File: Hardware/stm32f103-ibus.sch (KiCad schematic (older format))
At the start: 23 parts

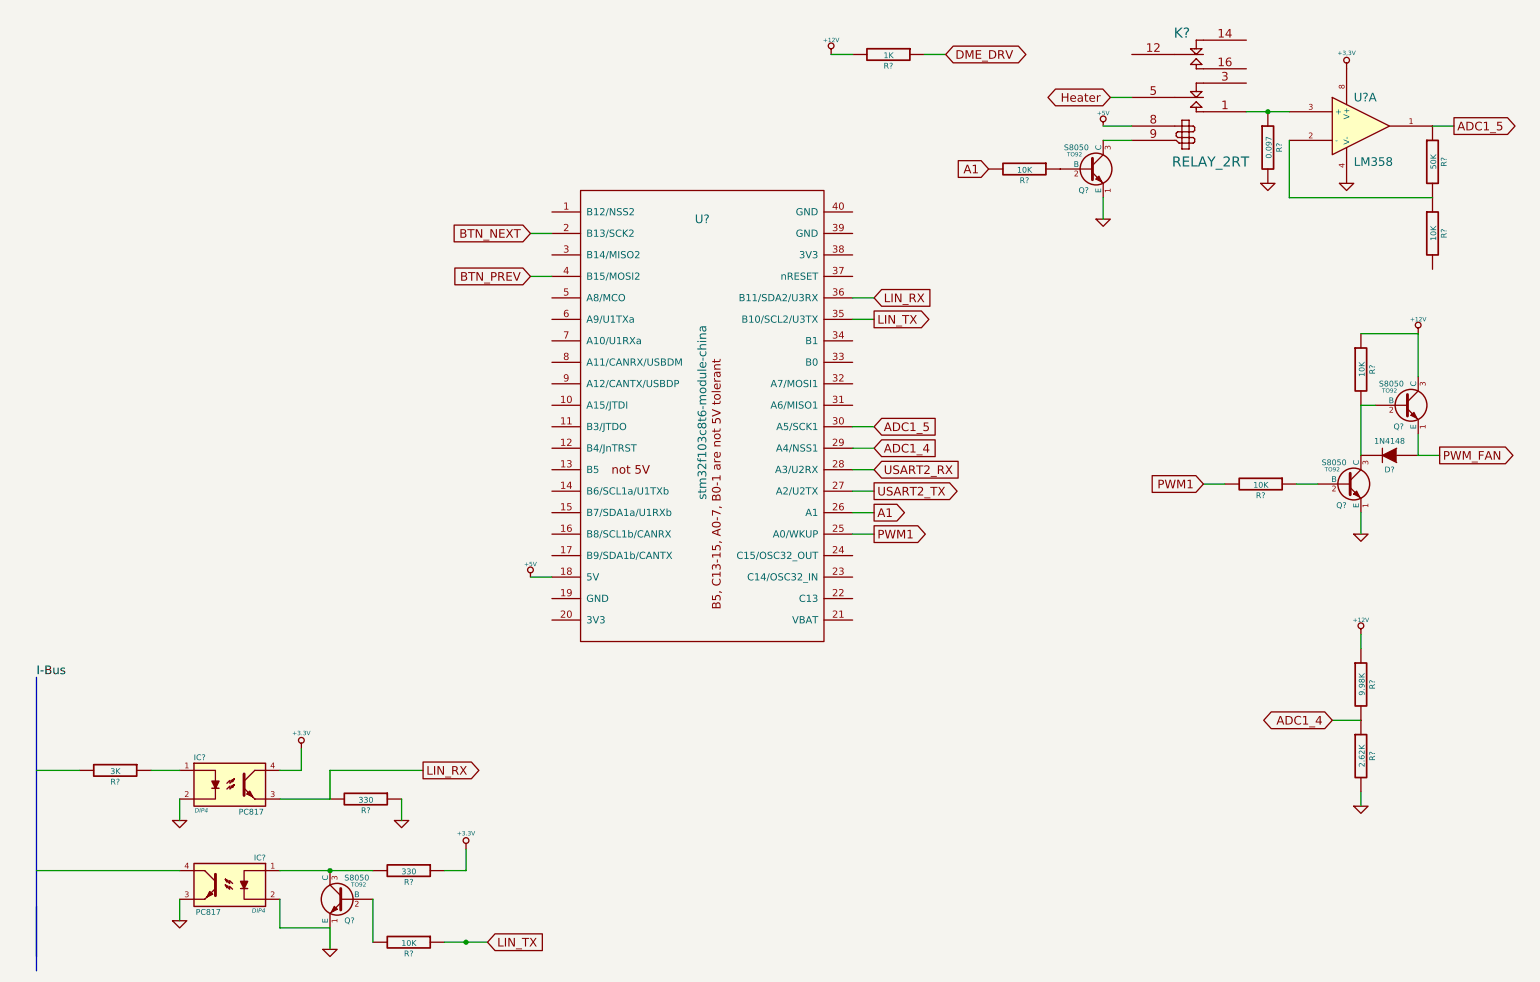
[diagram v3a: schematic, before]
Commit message: 1.Remove Hardware/stm32f103-ibus.bak 2.Modify of schematic 3.Force heater off while heater current over 2A 4.Modify logic of target temperature compensation 5.Add License
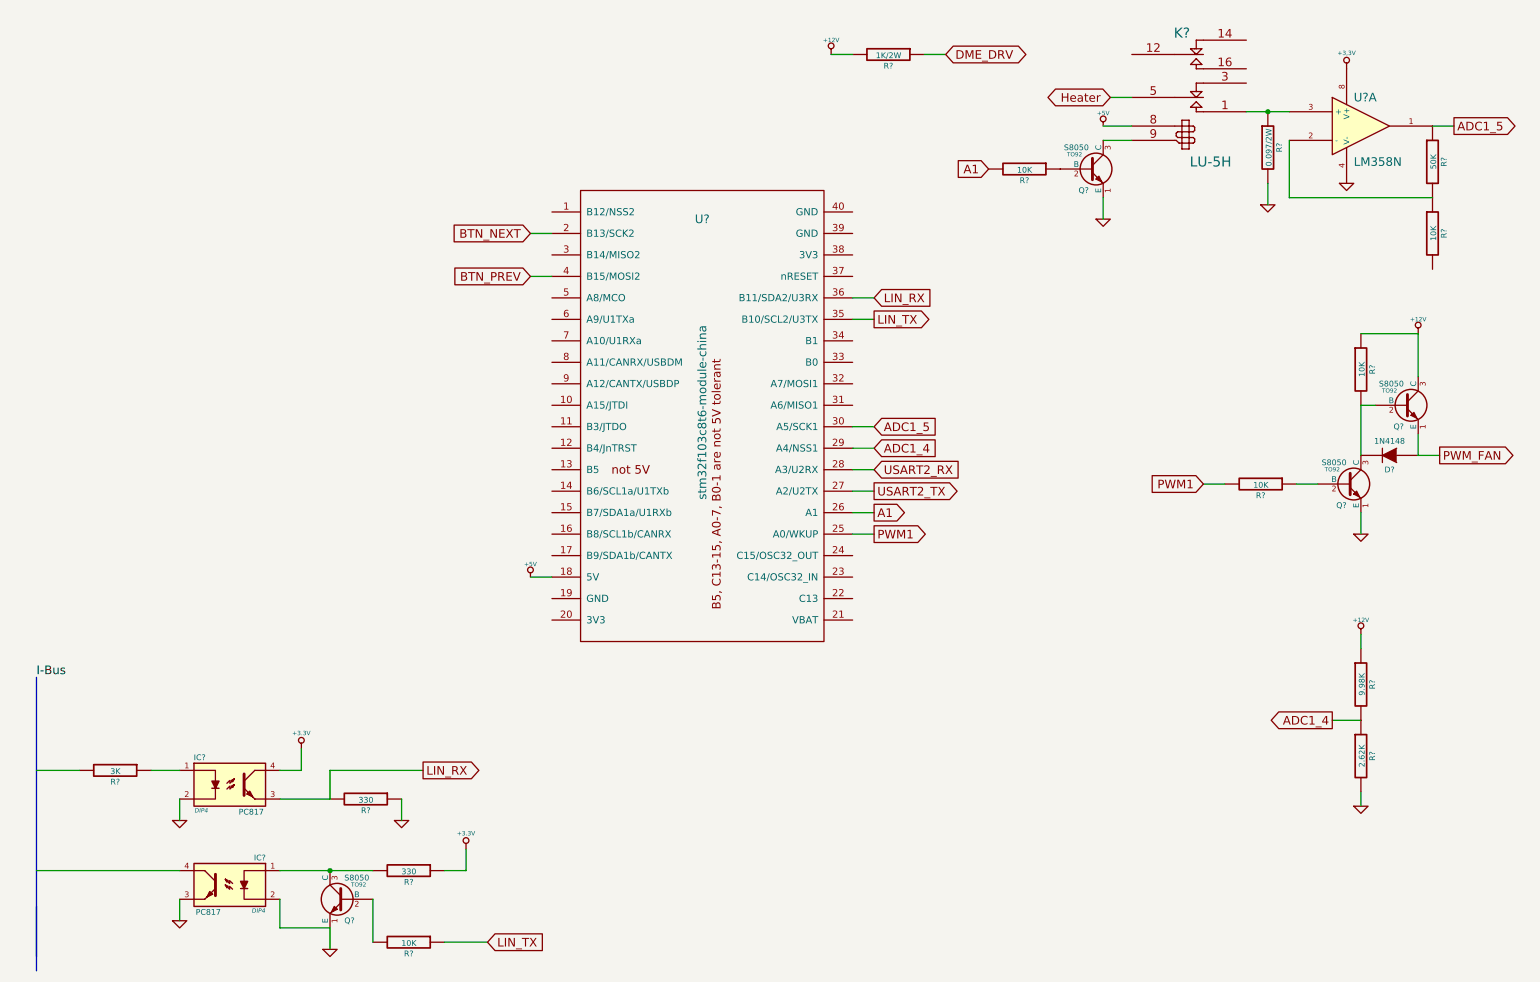
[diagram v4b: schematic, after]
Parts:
- K?: value RELAY_2RT -> LU-5H
- R?: value 1K -> 1K/2W
- R?: value 0.097 -> 0.097/2W
- U?: value LM358 -> LM358N
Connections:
- wire segments 52 -> 53
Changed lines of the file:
@@
 	1    0    0    -1
 $EndComp
-Text GLabel 9850 5600 0    60   BiDi ~ 0
+Text GLabel 9850 5600 0    60   Output ~ 0
 ADC1_4
 Text GLabel 8300 1250 0    60   BiDi ~ 0
@@
 P 6750 950
 F 0 "R?" V 6830 950 40  0000 C CNN
-F 1 "1K" V 6757 951 40  0000 C CNN
+F 1 "1K/2W" V 6757 951 40  0000 C CNN
 F 2 "" V 6680 950 30  0000 C CNN
 F 3 "" H 6750 950 30  0000 C CNN
@@
 P 8850 1200
 F 0 "K?" H 8800 1600 70  0000 C CNN
-F 1 "RELAY_2RT" H 9000 700 70  0000 C CNN
+F 1 "LU-5H" H 9000 700 70  0000 C CNN
 F 2 "" H 8850 1200 60  0000 C CNN
 F 3 "" H 8850 1200 60  0000 C CNN
@@
 P 10050 1450
 F 0 "U?" H 10000 1650 60  0000 L CNN
-F 1 "LM358" H 10000 1200 60  0000 L CNN
+F 1 "LM358N" H 10000 1200 60  0000 L CNN
 F 2 "" H 10050 1450 60  0000 C CNN
 F 3 "" H 10050 1450 60  0000 C CNN
@@
 $EndComp
 $Comp
-L GND #PWR?
-U 1 1 59957459
-P 9400 1850
-F 0 "#PWR?" H 9400 1850 30  0001 C CNN
-F 1 "GND" H 9400 1780 30  0001 C CNN
-F 2 "" H 9400 1850 60  0000 C CNN
-F 3 "" H 9400 1850 60  0000 C CNN
-	1    9400 1850
+L R R?
+U 1 1 599587F4
+P 9400 1600
+F 0 "R?" V 9480 1600 40  0000 C CNN
+F 1 "0.097/2W" V 9407 1601 40  0000 C CNN
+F 2 "" V 9330 1600 30  0000 C CNN
+F 3 "" H 9400 1600 30  0000 C CNN
+	1    9400 1600
 	1    0    0    -1
 $EndComp
@@
 	3150 6850 3150 7150
 Wire Wire Line
+	3650 6650 3800 6650
+Wire Wire Line
+	3800 6650 3800 6500
+Wire Wire Line
+	2850 7050 2850 7200
+Wire Wire Line
+	2500 6850 2500 7050
+Wire Wire Line
+	2500 7050 2850 7050
+Wire Wire Line
+	1800 6850 1800 7000
+Wire Wire Line
+	6500 2650 6650 2650
+Wire Wire Line
+	6500 2800 6650 2800
+Wire Wire Line
+	6500 3850 6650 3850
+Wire Wire Line
+	6500 4000 6650 4000
+Wire Wire Line
+	3350 6150 3350 6300
+Wire Wire Line
+	6500 3700 6650 3700
+Wire Wire Line
+	10050 5000 10050 5100
+Wire Wire Line
+	10050 6100 10050 6200
+Wire Wire Line
+	9850 5600 10050 5600
+Wire Wire Line
+	8250 1950 8250 2100
+Wire Wire Line
+	8250 1550 8450 1550
+Wire Wire Line
+	8250 1450 8450 1450
+Wire Wire Line
+	6500 950  6350 950
+Wire Wire Line
+	6650 4300 6500 4300
+Wire Wire Line
+	6650 4150 6500 4150
+Wire Wire Line
+	7000 950  7150 950
+Wire Wire Line
+	8300 1250 8450 1250
+Wire Wire Line
+	4400 4600 4250 4600
+Wire Wire Line
+	10450 2900 10050 2900
+Wire Wire Line
+	10050 3400 10150 3400
+Wire Wire Line
+	10450 2900 10450 3200
+Wire Wire Line
+	10050 3400 10050 3750
+Wire Wire Line
+	10450 3600 10450 3750
+Wire Wire Line
+	8950 3950 9100 3950
+Wire Wire Line
+	9600 3950 9750 3950
+Wire Wire Line
+	10050 4150 10050 4300
+Wire Wire Line
+	10450 3750 10600 3750
+Wire Wire Line
+	4250 2200 4400 2200
+Wire Wire Line
+	4250 2500 4400 2500
+Wire Wire Line
+	6500 3550 6650 3550
+Wire Wire Line
+	10700 1450 10550 1450
+Wire Wire Line
+	9550 1550 9550 1950
+Wire Wire Line
+	9550 1950 10550 1950
+Wire Wire Line
+	2500 6150 2850 6150
+Wire Wire Line
+	3500 5950 2850 5950
+Wire Wire Line
+	2850 5950 2850 6150
+Wire Wire Line
+	3950 7150 3650 7150
+Wire Wire Line
 	2500 6650 3150 6650
 Connection ~ 2850 6650
 Wire Wire Line
-	3650 6650 3800 6650
-Wire Wire Line
-	3650 7150 3950 7150
-Connection ~ 3800 7150
-Wire Wire Line
-	3800 6650 3800 6500
-Wire Wire Line
-	2850 7050 2850 7200
-Wire Wire Line
-	2500 6850 2500 7050
-Wire Wire Line
-	2500 7050 2850 7050
-Wire Wire Line
-	1800 6850 1800 7000
-Wire Wire Line
-	6500 2650 6650 2650
-Wire Wire Line
-	6500 2800 6650 2800
-Wire Wire Line
-	6500 3850 6650 3850
-Wire Wire Line
-	6500 4000 6650 4000
-Wire Wire Line
-	2500 6150 2850 6150
-Wire Wire Line
-	2850 6150 2850 5950
-Wire Wire Line
-	2850 5950 3500 5950
-Wire Wire Line
-	3350 6150 3350 6300
-Wire Wire Line
-	6500 3700 6650 3700
-Wire Wire Line
-	10050 5000 10050 5100
-Wire Wire Line
-	10050 6100 10050 6200
-Wire Wire Line
-	9850 5600 10050 5600
-Wire Wire Line
-	8250 1950 8250 2100
-Wire Wire Line
-	8250 1550 8450 1550
-Wire Wire Line
-	8250 1450 8450 1450
-Wire Wire Line
-	6500 950  6350 950
-Wire Wire Line
-	6650 4300 6500 4300
-Wire Wire Line
-	6650 4150 6500 4150
-Wire Wire Line
-	7000 950  7150 950
-Wire Wire Line
-	8300 1250 8450 1250
-Wire Wire Line
-	4400 4600 4250 4600
-Wire Wire Line
-	10450 2900 10050 2900
-Wire Wire Line
-	10050 3400 10150 3400
-Wire Wire Line
-	10450 2900 10450 3200
-Wire Wire Line
-	10050 3400 10050 3750
-Wire Wire Line
-	10450 3600 10450 3750
-Wire Wire Line
-	8950 3950 9100 3950
-Wire Wire Line
-	9600 3950 9750 3950
-Wire Wire Line
-	10050 4150 10050 4300
-Wire Wire Line
-	10450 3750 10600 3750
-Wire Wire Line
-	4250 2200 4400 2200
-Wire Wire Line
-	4250 2500 4400 2500
-Wire Wire Line
-	6500 3550 6650 3550
-Wire Wire Line
-	10700 1450 10550 1450
-Wire Wire Line
-	9550 1550 9550 1950
-Wire Wire Line
-	9550 1950 10550 1950
-$Comp
-L R R?
-U 1 1 599587F4
-P 9400 1600
-F 0 "R?" V 9480 1600 40  0000 C CNN
-F 1 "0.097" V 9407 1601 40  0000 C CNN
-F 2 "" V 9330 1600 30  0000 C CNN
-F 3 "" H 9400 1600 30  0000 C CNN
-	1    9400 1600
-	1    0    0    -1
-$EndComp
-Wire Wire Line
 	9250 1350 9550 1350
 Connection ~ 9400 1350
+$Comp
+L GND #PWR?
+U 1 1 59A94DBE
+P 9400 2000
+F 0 "#PWR?" H 9400 2000 30  0001 C CNN
+F 1 "GND" H 9400 1930 30  0001 C CNN
+F 2 "" H 9400 2000 60  0000 C CNN
+F 3 "" H 9400 2000 60  0000 C CNN
+	1    9400 2000
+	1    0    0    -1
+$EndComp
+Wire Wire Line
+	9400 1850 9400 2000
 $EndSCHEMATC

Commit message: 1.Add connector to schematic 2.Remove NEXT_BTN / PREV_BTN of schematic
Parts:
- added P?: USART2, symbol CONN_01X04
- added P?: POWER, symbol CONN_01X02
- added P?: I-Bus, symbol CONN_01X01
- added P?: HEATER, symbol CONN_01X01
- added P?: PWM_FAN, symbol CONN_01X01
- added P?: DME_DRV, symbol CONN_01X01
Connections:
- net labels added: HEATER
- net labels removed: BTN_NEXT, BTN_PREV, Heater
- wire segments 53 -> 64
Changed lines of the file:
@@
 ADC1_4
 Text GLabel 8300 1250 0    60   BiDi ~ 0
-Heater
+HEATER
 $Comp
 L S8050 Q?
@@
 Text GLabel 6650 3550 2    60   Input ~ 0
 ADC1_5
-Text GLabel 4250 2200 0    60   Input ~ 0
-BTN_NEXT
-Text GLabel 4250 2500 0    60   Input ~ 0
-BTN_PREV
 $Comp
 L LM358 U?
@@
 	1    0    0    -1
 $EndComp
-Wire Bus Line
-	800  5300 800  7250
-Wire Bus Line
-	800  6900 800  7350
-Wire Wire Line
-	800  5950 1100 5950
-Wire Wire Line
-	1600 5950 1800 5950
-Wire Wire Line
-	1800 6150 1800 6300
-Wire Wire Line
-	2500 5950 2650 5950
-Wire Wire Line
-	2650 5950 2650 5800
-Wire Wire Line
-	800  6650 1800 6650
-Wire Wire Line
-	3150 6850 3150 7150
-Wire Wire Line
-	3650 6650 3800 6650
-Wire Wire Line
-	3800 6650 3800 6500
-Wire Wire Line
-	2850 7050 2850 7200
-Wire Wire Line
-	2500 6850 2500 7050
-Wire Wire Line
-	2500 7050 2850 7050
-Wire Wire Line
-	1800 6850 1800 7000
-Wire Wire Line
-	6500 2650 6650 2650
-Wire Wire Line
-	6500 2800 6650 2800
-Wire Wire Line
-	6500 3850 6650 3850
-Wire Wire Line
-	6500 4000 6650 4000
-Wire Wire Line
-	3350 6150 3350 6300
-Wire Wire Line
-	6500 3700 6650 3700
-Wire Wire Line
-	10050 5000 10050 5100
-Wire Wire Line
-	10050 6100 10050 6200
-Wire Wire Line
-	9850 5600 10050 5600
-Wire Wire Line
-	8250 1950 8250 2100
-Wire Wire Line
-	8250 1550 8450 1550
-Wire Wire Line
-	8250 1450 8450 1450
-Wire Wire Line
-	6500 950  6350 950
-Wire Wire Line
-	6650 4300 6500 4300
-Wire Wire Line
-	6650 4150 6500 4150
-Wire Wire Line
-	7000 950  7150 950
-Wire Wire Line
-	8300 1250 8450 1250
-Wire Wire Line
-	4400 4600 4250 4600
-Wire Wire Line
-	10450 2900 10050 2900
-Wire Wire Line
-	10050 3400 10150 3400
-Wire Wire Line
-	10450 2900 10450 3200
-Wire Wire Line
-	10050 3400 10050 3750
-Wire Wire Line
-	10450 3600 10450 3750
-Wire Wire Line
-	8950 3950 9100 3950
-Wire Wire Line
-	9600 3950 9750 3950
-Wire Wire Line
-	10050 4150 10050 4300
-Wire Wire Line
-	10450 3750 10600 3750
-Wire Wire Line
-	4250 2200 4400 2200
-Wire Wire Line
-	4250 2500 4400 2500
-Wire Wire Line
-	6500 3550 6650 3550
-Wire Wire Line
-	10700 1450 10550 1450
-Wire Wire Line
-	9550 1550 9550 1950
-Wire Wire Line
-	9550 1950 10550 1950
-Wire Wire Line
-	2500 6150 2850 6150
-Wire Wire Line
-	3500 5950 2850 5950
-Wire Wire Line
-	2850 5950 2850 6150
-Wire Wire Line
-	3950 7150 3650 7150
-Wire Wire Line
-	2500 6650 3150 6650
-Connection ~ 2850 6650
-Wire Wire Line
-	9250 1350 9550 1350
-Connection ~ 9400 1350
 $Comp
 L GND #PWR?
@@
 	1    0    0    -1
 $EndComp
+$Comp
+L CONN_01X04 P?
+U 1 1 59AF8F34
+P 850 950
+F 0 "P?" H 850 1200 50  0000 C CNN
+F 1 "USART2" V 950 950 50  0000 C CNN
+F 2 "" H 850 950 60  0000 C CNN
+F 3 "" H 850 950 60  0000 C CNN
+	1    850  950
+	-1   0    0    -1
+$EndComp
+$Comp
+L +3.3V #PWR?
+U 1 1 59AF94A8
+P 1200 800
+F 0 "#PWR?" H 1200 760 30  0001 C CNN
+F 1 "+3.3V" H 1200 910 30  0000 C CNN
+F 2 "" H 1200 800 60  0000 C CNN
+F 3 "" H 1200 800 60  0000 C CNN
+	1    1200 800
+	1    0    0    -1
+$EndComp
+$Comp
+L GND #PWR?
+U 1 1 59AF94BC
+P 1050 1250
+F 0 "#PWR?" H 1050 1250 30  0001 C CNN
+F 1 "GND" H 1050 1180 30  0001 C CNN
+F 2 "" H 1050 1250 60  0000 C CNN
+F 3 "" H 1050 1250 60  0000 C CNN
+	1    1050 1250
+	1    0    0    -1
+$EndComp
+Text GLabel 1350 1100 2    60   Input ~ 0
+USART2_TX
+Text GLabel 1200 900  2    60   Output ~ 0
+USART2_RX
+$Comp
+L CONN_01X02 P?
+U 1 1 59AFA389
+P 850 1600
+F 0 "P?" H 850 1750 50  0000 C CNN
+F 1 "POWER" V 950 1600 50  0000 C CNN
+F 2 "" H 850 1600 60  0000 C CNN
+F 3 "" H 850 1600 60  0000 C CNN
+	1    850  1600
+	-1   0    0    -1
+$EndComp
+$Comp
+L +12V #PWR?
+U 1 1 59AFA45F
+P 1200 1550
+F 0 "#PWR?" H 1200 1500 20  0001 C CNN
+F 1 "+12V" H 1200 1650 30  0000 C CNN
+F 2 "" H 1200 1550 60  0000 C CNN
+F 3 "" H 1200 1550 60  0000 C CNN
+	1    1200 1550
+	1    0    0    -1
+$EndComp
+$Comp
+L GND #PWR?
+U 1 1 59AFA473
+P 1200 1750
+F 0 "#PWR?" H 1200 1750 30  0001 C CNN
+F 1 "GND" H 1200 1680 30  0001 C CNN
+F 2 "" H 1200 1750 60  0000 C CNN
+F 3 "" H 1200 1750 60  0000 C CNN
+	1    1200 1750
+	1    0    0    -1
+$EndComp
+$Comp
+L CONN_01X01 P?
+U 1 1 59AFA583
+P 850 2050
+F 0 "P?" H 850 2150 50  0000 C CNN
+F 1 "I-Bus" V 950 2050 50  0000 C CNN
+F 2 "" H 850 2050 60  0000 C CNN
+F 3 "" H 850 2050 60  0000 C CNN
+	1    850  2050
+	-1   0    0    -1
+$EndComp
+$Comp
+L CONN_01X01 P?
+U 1 1 59AFA59E
+P 850 2500
+F 0 "P?" H 850 2600 50  0000 C CNN
+F 1 "HEATER" V 950 2500 50  0000 C CNN
+F 2 "" H 850 2500 60  0000 C CNN
+F 3 "" H 850 2500 60  0000 C CNN
+	1    850  2500
+	-1   0    0    -1
+$EndComp
+Wire Bus Line
+	800  5300 800  7250
+Wire Bus Line
+	800  6900 800  7350
+Wire Wire Line
+	800  5950 1100 5950
+Wire Wire Line
+	1600 5950 1800 5950
+Wire Wire Line
+	1800 6150 1800 6300
+Wire Wire Line
+	2500 5950 2650 5950
+Wire Wire Line
+	2650 5950 2650 5800
+Wire Wire Line
+	800  6650 1800 6650
+Wire Wire Line
+	3150 6850 3150 7150
+Wire Wire Line
+	3650 6650 3800 6650
+Wire Wire Line
+	3800 6650 3800 6500
+Wire Wire Line
+	2850 7050 2850 7200
+Wire Wire Line
+	2500 6850 2500 7050
+Wire Wire Line
+	2500 7050 2850 7050
+Wire Wire Line
+	1800 6850 1800 7000
+Wire Wire Line
+	6500 2650 6650 2650
+Wire Wire Line
+	6500 2800 6650 2800
+Wire Wire Line
+	6500 3850 6650 3850
+Wire Wire Line
+	6500 4000 6650 4000
+Wire Wire Line
+	3350 6150 3350 6300
+Wire Wire Line
+	6500 3700 6650 3700
+Wire Wire Line
+	10050 5000 10050 5100
+Wire Wire Line
+	10050 6100 10050 6200
+Wire Wire Line
+	9850 5600 10050 5600
+Wire Wire Line
+	8250 1950 8250 2100
+Wire Wire Line
+	8250 1550 8450 1550
+Wire Wire Line
+	8250 1450 8450 1450
+Wire Wire Line
+	6500 950  6350 950
+Wire Wire Line
+	6650 4300 6500 4300
+Wire Wire Line
+	6650 4150 6500 4150
+Wire Wire Line
+	7000 950  7150 950
+Wire Wire Line
+	8300 1250 8450 1250
+Wire Wire Line
+	4400 4600 4250 4600
+Wire Wire Line
+	10450 2900 10050 2900
+Wire Wire Line
+	10050 3400 10150 3400
+Wire Wire Line
+	10450 2900 10450 3200
+Wire Wire Line
+	10050 3400 10050 3750
+Wire Wire Line
+	10450 3600 10450 3750
+Wire Wire Line
+	8950 3950 9100 3950
+Wire Wire Line
+	9600 3950 9750 3950
+Wire Wire Line
+	10050 4150 10050 4300
+Wire Wire Line
+	10450 3750 10600 3750
+Wire Wire Line
+	6500 3550 6650 3550
+Wire Wire Line
+	10700 1450 10550 1450
+Wire Wire Line
+	9550 1550 9550 1950
+Wire Wire Line
+	9550 1950 10550 1950
+Wire Wire Line
+	2500 6150 2850 6150
+Wire Wire Line
+	3500 5950 2850 5950
+Wire Wire Line
+	2850 5950 2850 6150
+Wire Wire Line
+	3950 7150 3650 7150
+Wire Wire Line
+	2500 6650 3150 6650
+Connection ~ 2850 6650
+Wire Wire Line
+	9250 1350 9550 1350
+Connection ~ 9400 1350
 Wire Wire Line
 	9400 1850 9400 2000
+Wire Wire Line
+	1050 800  1200 800
+Wire Wire Line
+	1050 1000 1200 1000
+Wire Wire Line
+	1200 1000 1200 1100
+Wire Wire Line
+	1050 900  1200 900
+Wire Wire Line
+	1200 1100 1350 1100
+Wire Wire Line
+	1050 1100 1050 1250
+Wire Wire Line
+	1050 1550 1200 1550
+Wire Wire Line
+	1050 1650 1200 1650
+Wire Wire Line
+	1200 1650 1200 1750
+Wire Bus Line
+	1500 1900 1500 2250
+Text Label 1500 2050 0    60   ~ 0
+I-Bus
+Wire Wire Line
+	1050 2050 1500 2050
+Text GLabel 1200 2500 2    60   BiDi ~ 0
+HEATER
+Wire Wire Line
+	1050 2500 1200 2500
+$Comp
+L CONN_01X01 P?
+U 1 1 59AFBA4B
+P 850 2950
+F 0 "P?" H 850 3050 50  0000 C CNN
+F 1 "PWM_FAN" V 950 2950 50  0000 C CNN
+F 2 "" H 850 2950 60  0000 C CNN
+F 3 "" H 850 2950 60  0000 C CNN
+	1    850  2950
+	-1   0    0    -1
+$EndComp
+Text GLabel 1200 2950 2    60   Input ~ 0
+PWM_FAN
+Wire Wire Line
+	1200 2950 1050 2950
+$Comp
+L CONN_01X01 P?
+U 1 1 59AFC60B
+P 850 3450
+F 0 "P?" H 850 3550 50  0000 C CNN
+F 1 "DME_DRV" V 950 3450 50  0000 C CNN
+F 2 "" H 850 3450 60  0000 C CNN
+F 3 "" H 850 3450 60  0000 C CNN
+	1    850  3450
+	-1   0    0    -1
+$EndComp
+Text GLabel 1200 3450 2    60   BiDi ~ 0
+DME_DRV
+Wire Wire Line
+	1050 3450 1200 3450
 $EndSCHEMATC

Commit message: Modify schematic
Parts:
- K?: value LU-5H -> LU-3H
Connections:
- net +3.3V: now also K?.8
- net +5V: no longer names the net of U?.18 (5V)
- net +5V: no longer K?.8
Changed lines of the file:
@@
-$EndComp
-$Comp
-L +5V #PWR?
-U 1 1 597B2F4A
-P 8250 1450
-F 0 "#PWR?" H 8250 1540 20  0001 C CNN
-F 1 "+5V" H 8250 1540 30  0000 C CNN
-F 2 "" H 8250 1450 60  0000 C CNN
-F 3 "" H 8250 1450 60  0000 C CNN
-	1    8250 1450
-	1    0    0    -1
 $EndComp
 $Comp
@@
 P 8850 1200
 F 0 "K?" H 8800 1600 70  0000 C CNN
-F 1 "LU-5H" H 9000 700 70  0000 C CNN
+F 1 "LU-3H" H 9000 700 70  0000 C CNN
 F 2 "" H 8850 1200 60  0000 C CNN
 F 3 "" H 8850 1200 60  0000 C CNN
 	1    8850 1200
-	1    0    0    -1
-$EndComp
-$Comp
-L +5V #PWR?
-U 1 1 598D88F3
-P 4250 4600
-F 0 "#PWR?" H 4250 4690 20  0001 C CNN
-F 1 "+5V" H 4250 4690 30  0000 C CNN
-F 2 "" H 4250 4600 60  0000 C CNN
-F 3 "" H 4250 4600 60  0000 C CNN
-	1    4250 4600
 	1    0    0    -1
 $EndComp
@@
 	8250 1550 8450 1550
 Wire Wire Line
-	8250 1450 8450 1450
-Wire Wire Line
 	6500 950  6350 950
 Wire Wire Line
@@
 Wire Wire Line
 	8300 1250 8450 1250
-Wire Wire Line
-	4400 4600 4250 4600
 Wire Wire Line
 	10450 2900 10050 2900
@@
 Wire Wire Line
 	1050 3450 1200 3450
+$Comp
+L +3.3V #PWR?
+U 1 1 59AFE060
+P 8250 1450
+F 0 "#PWR?" H 8250 1410 30  0001 C CNN
+F 1 "+3.3V" H 8250 1560 30  0000 C CNN
+F 2 "" H 8250 1450 60  0000 C CNN
+F 3 "" H 8250 1450 60  0000 C CNN
+	1    8250 1450
+	1    0    0    -1
+$EndComp
+Wire Wire Line
+	8450 1450 8250 1450
 $EndSCHEMATC
